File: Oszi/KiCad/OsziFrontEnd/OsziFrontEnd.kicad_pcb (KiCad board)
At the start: 2 copper layers, 91.9 x 85.4 mm, 42 parts, among them J1 Conn_Coaxial, J2 Conn_Coaxial, J3 Conn_01x03_Pin, J4 Conn_01x03_Pin, J5 USB_C_Receptacle_PowerOnly_6P, U1 MCP6002-xP, U2 MCP6002-xP, U3 NUCLEO-L432KC, U4 TPS62160DGK, U6 CR2013-MI2120

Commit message: finsihed layout
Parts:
- moved J2 13.5 mm to (98.5, 94.4)
- moved R9 6.50 mm to (103.2, 83.8)
- moved J4 6.09 mm to (94.1, 83.6)
- moved R17 6.09 mm to (103.9, 82.2)
- moved R8 6.09 mm to (97.2, 83.2)
- moved R10 6.09 mm to (101.5, 86.0)
- moved R11 6.09 mm to (97.3, 86.2)
- moved R7 6.09 mm to (100.0, 82.9)
- moved CH Select 6.02 mm to (145.8, 75.7)
- moved Mode Select 5.97 mm to (145.6, 84.9)
- moved Run / Stop 5.76 mm to (145.8, 67.0)
- moved Trimm 5.73 mm to (146.4, 94.5)
- moved U3 5.64 mm to (138.3, 97.7)
- moved J1 2.02 mm to (86.0, 80.5)
- moved C2 1.76 mm to (88.6, 69.0)
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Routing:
- net 3V3: track 237.8 -> 254.2 mm
- net /Display/DD/C: track 83.5 -> 75.7 mm
- net /Display/DSCK: track 78.4 -> 72.0 mm
- net /AnalogesFrontEnd/ADC_CH1_1V: track 26.2 -> 20.5 mm
- net /AnalogesFrontEnd/ADC_CH1_10V: track 16.7 -> 11.1 mm
- net /AnalogesFrontEnd/ADC_CH2_36V: track 27.8 -> 22.1 mm
- net /Display/DMOSI: track 76.7 -> 71.8 mm
- net /Display/DRs: track 77.8 -> 72.9 mm
- net /Display/DMISO: track 71.1 -> 66.4 mm
- net Net-(U2A-+): track 2.63 -> 7.32 mm
- net /AnalogesFrontEnd/ADC_CH2_10V: track 19.3 -> 15.0 mm
- net /Display/DCS: track 92.7 -> 88.9 mm
- net /AnalogesFrontEnd/Vout-10;10CH2: track 17.9 -> 21.4 mm
- net GNDD: track 17.3 -> 19.7 mm, vias 0 -> 1
- net /AnalogesFrontEnd/CoaxCH2: track 10.8 -> 13.0 mm
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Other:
- board size 91.9 x 85.4 mm -> 75.3 x 85.4 mm

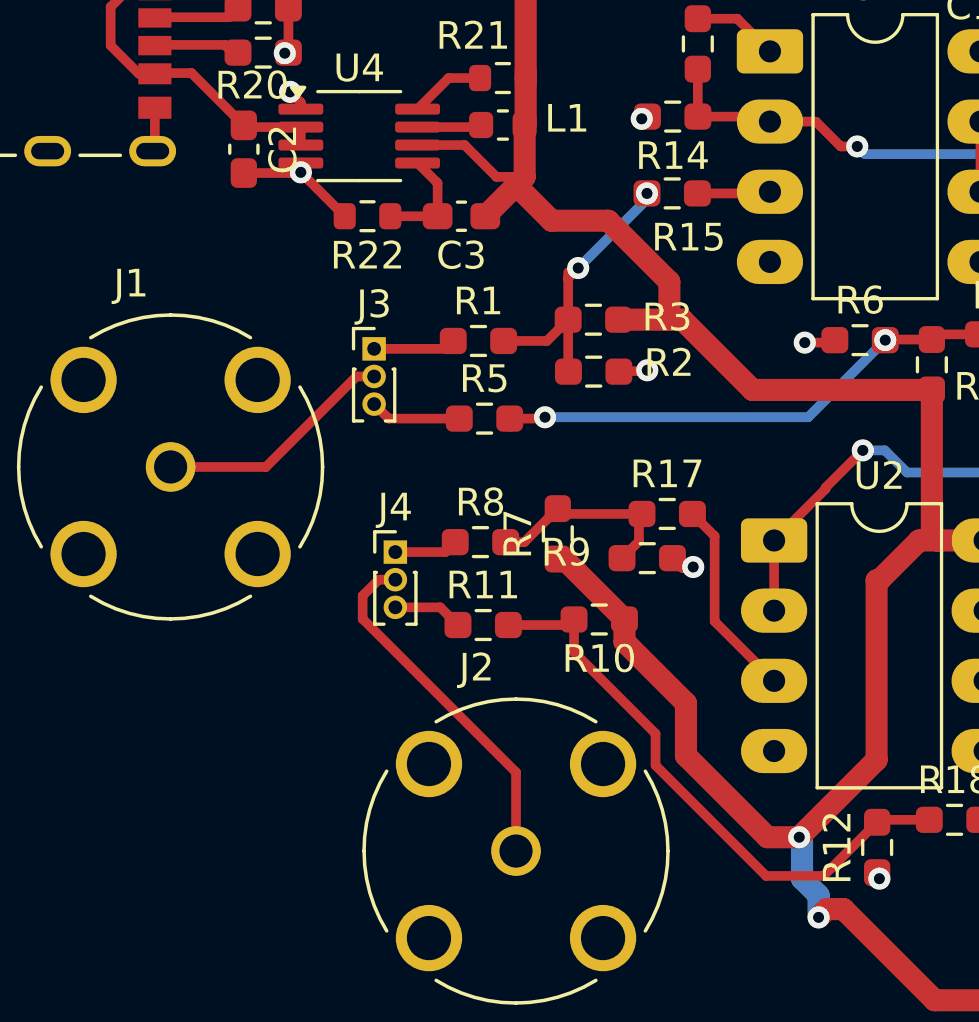
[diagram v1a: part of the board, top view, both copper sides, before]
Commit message: fixed spacing on pcb
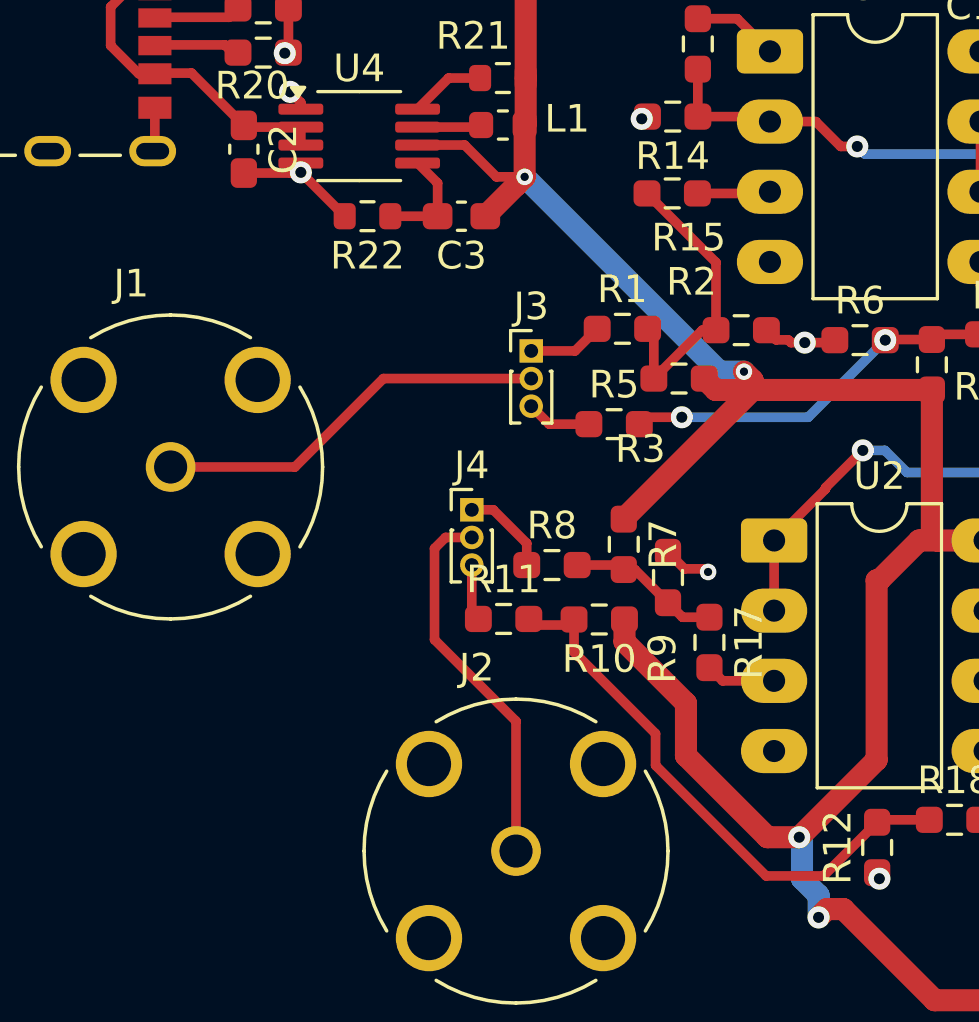
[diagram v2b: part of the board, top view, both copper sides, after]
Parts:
- moved J3 5.69 mm to (99.0, 76.3)
- moved R2 5.55 mm to (106.6, 75.5)
- moved R1 5.23 mm to (102.3, 75.5)
- moved R17 4.89 mm to (105.5, 86.8), turned to -90 degrees
- moved R5 4.69 mm to (102.0, 79.0)
- moved R3 3.76 mm to (104.3, 77.3)
- moved J4 3.16 mm to (96.8, 82.0)
- moved R8 2.72 mm to (99.8, 84.0)
- moved R7 2.42 mm to (102.3, 83.3), turned to -90 degrees
- moved R9 1.03 mm to (104.0, 84.5), turned to -90 degrees
- moved R11 0.77 mm to (98.0, 86.0)
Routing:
- net /AnalogesFrontEnd/CoaxCH1: track 8.72 -> 14.4 mm
- net /AnalogesFrontEnd/Vout-10;10CH1: track 18.5 -> 13.6 mm
- net Net-(U2A-+): track 7.32 -> 2.54 mm
- net 3V3: track 254.2 -> 256.8 mm, vias 2 -> 4
- net /AnalogesFrontEnd/Vout-36;36CH2: track 7.42 -> 5.57 mm
- net GND: track 19.1 -> 20.5 mm, vias 10 -> 9
- net /AnalogesFrontEnd/Vin-36;36CH2: track 2.32 -> 3.28 mm
- net /AnalogesFrontEnd/Vin-10;10CH1: track 3.30 -> 2.36 mm
- net /AnalogesFrontEnd/CoaxCH2: track 13.0 -> 13.7 mm
- net /AnalogesFrontEnd/Vout-10;10CH2: track 21.4 -> 20.7 mm
- net /AnalogesFrontEnd/Vout-1;1CH1: track 10.5 -> 10.9 mm, vias 2 -> 0

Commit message: jetzt git
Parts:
- removed CH Select: SW_Push, Button_Switch_SMD:SW_SPST_PTS645Sx43SMTR92
- removed Mode Select: SW_Push, Button_Switch_SMD:SW_SPST_PTS645Sx43SMTR92
- removed Run / Stop: SW_Push, Button_Switch_SMD:SW_SPST_PTS645Sx43SMTR92
- removed Trimm: R_Potentiometer, Potentiometer_SMD:Potentiometer_ACP_CA6-VSMD_Vertical
- removed U6: CR2013-MI2120, Display:CR2013-MI2120
- added J6: Conn_01x14_Socket, Connector_PinSocket_2.54mm:PinSocket_1x14_P2.54mm_Vertical, F.Cu at (87.0, 20.9)
- added J7: Conn_01x04_Socket, Connector_PinSocket_2.54mm:PinSocket_1x04_P2.54mm_Vertical, F.Cu at (168.3, 33.6)
- added RV1: R_Potentiometer, Potentiometer_SMD:Potentiometer_ACP_CA6-VSMD_Vertical, F.Cu at (146.4, 89.7)
- added SW1: SW_Push, Button_Switch_SMD:SW_SPST_PTS645Sx43SMTR92, F.Cu at (145.6, 80.4)
- added SW2: SW_Push, Button_Switch_SMD:SW_SPST_PTS645Sx43SMTR92, F.Cu at (146.1, 71.6)
- added SW3: SW_Push, Button_Switch_SMD:SW_SPST_PTS645Sx43SMTR92, F.Cu at (145.9, 63.6)
- moved C4 7.45 mm to (83.7, 22.4)
- moved R23 4.46 mm to (83.7, 26.0)
- moved J4 3.60 mm to (100.5, 82.1), turned to -90 degrees
- moved R8 0.29 mm to (99.9, 84.3)
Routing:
- net 3V3: track 256.8 -> 276.6 mm
- net Net-(U3A-PA9): track 5.12 -> 15.8 mm, vias 0 -> 1
- net /AnalogesFrontEnd/Vin-10;10CH2: track 2.05 -> 4.80 mm
- net /Display/DRs: track 72.9 -> 70.8 mm
- net /Display/DD/C: track 75.7 -> 77.7 mm
- net /Display/DCS: track 88.9 -> 91.0 mm
- net GND: track 20.5 -> 22.4 mm
- net /Display/DMOSI: track 71.8 -> 73.6 mm, vias 0 -> 1
- net /Display/DMISO: track 66.4 -> 68.2 mm, vias 1 -> 2
- net /AnalogesFrontEnd/Vout-36;36CH2: track 5.57 -> 3.81 mm
- net /Display/DSCK: track 72.0 -> 73.6 mm
- net Net-(U3A-PB5): track 11.5 -> 13.0 mm
- net /AnalogesFrontEnd/CoaxCH2: track 13.7 -> 12.7 mm
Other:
- board size 75.3 x 85.4 mm -> 92.6 x 85.4 mm
